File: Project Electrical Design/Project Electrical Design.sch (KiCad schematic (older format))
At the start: 1 part

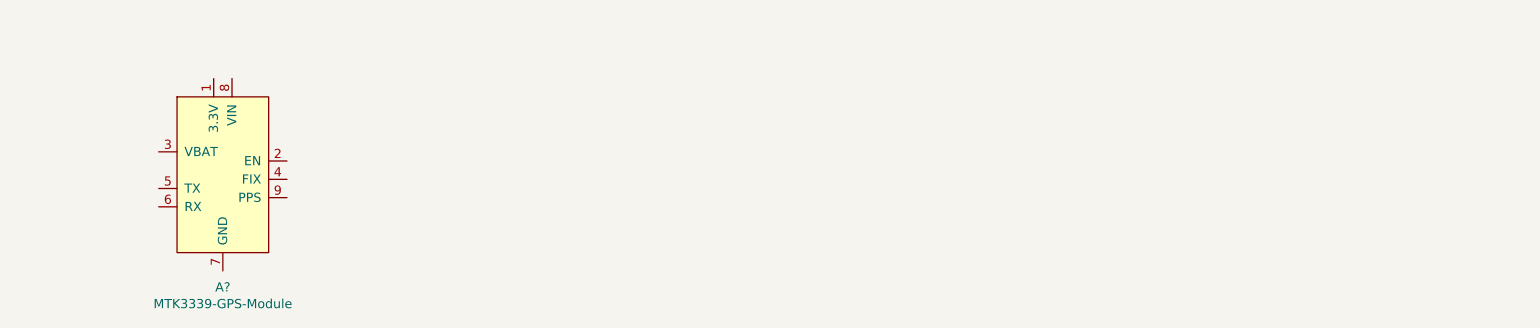
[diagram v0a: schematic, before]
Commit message: Added Adafruit I2C 7-seg part
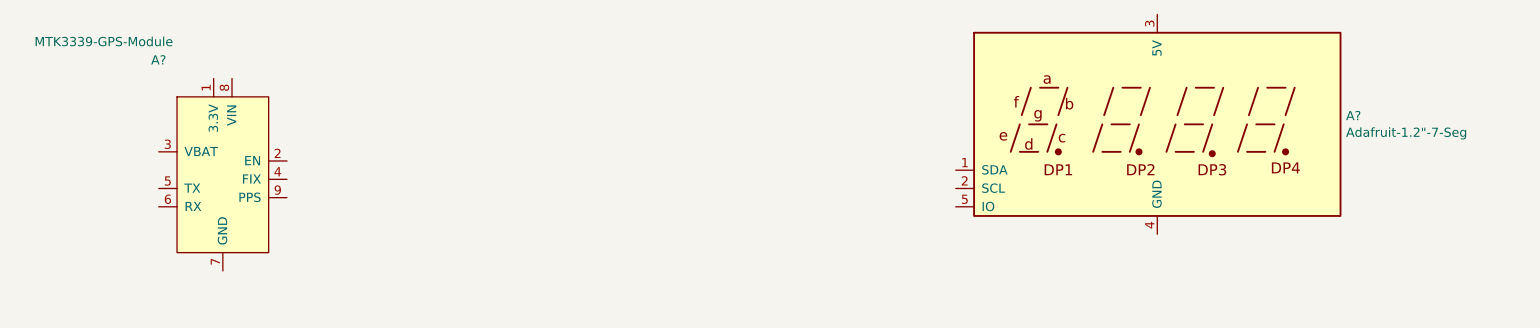
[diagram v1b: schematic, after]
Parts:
- added A?: Adafruit-1.2\"-7-Seg, symbol Adafruit-1.2-7-seg:Adafruit-1.2"-7-Seg
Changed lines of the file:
@@
 U 1 1 5E668337
 P 2650 2950
-F 0 "A?" H 2650 2361 50  0000 C CNN
-F 1 "MTK3339-GPS-Module" H 2650 2270 50  0000 C CNN
+F 0 "A?" H 2300 3600 50  0000 C CNN
+F 1 "MTK3339-GPS-Module" H 2000 3700 50  0000 C CNN
 F 2 "" H 2000 3700 50  0001 C CNN
 F 3 "" H 2000 3700 50  0001 C CNN
@@
 	1    0    0    -1
 $EndComp
+$Comp
+L Adafruit-1.2-7-seg:Adafruit-1.2"-7-Seg A?
+U 1 1 5E66F4C1
+P 7750 2700
+F 0 "A?" H 8780 2796 50  0000 L CNN
+F 1 "Adafruit-1.2\"-7-Seg" H 8780 2705 50  0000 L CNN
+F 2 "" H 6850 3500 50  0001 C CNN
+F 3 "" H 6850 3500 50  0001 C CNN
+	1    7750 2700
+	1    0    0    -1
+$EndComp
